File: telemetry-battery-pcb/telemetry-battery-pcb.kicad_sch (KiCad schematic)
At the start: 80 parts, among them J1 Network Connector, J3 360410_MZC, J4 DS18B20, J5 360410_MZC, Q4 2N7002, U4 LTC2944, U5 XR76208, U6 M24C02-WMN, U7 TPS1HTC30-Q1, U8 DS2484R, U9 TPS22969

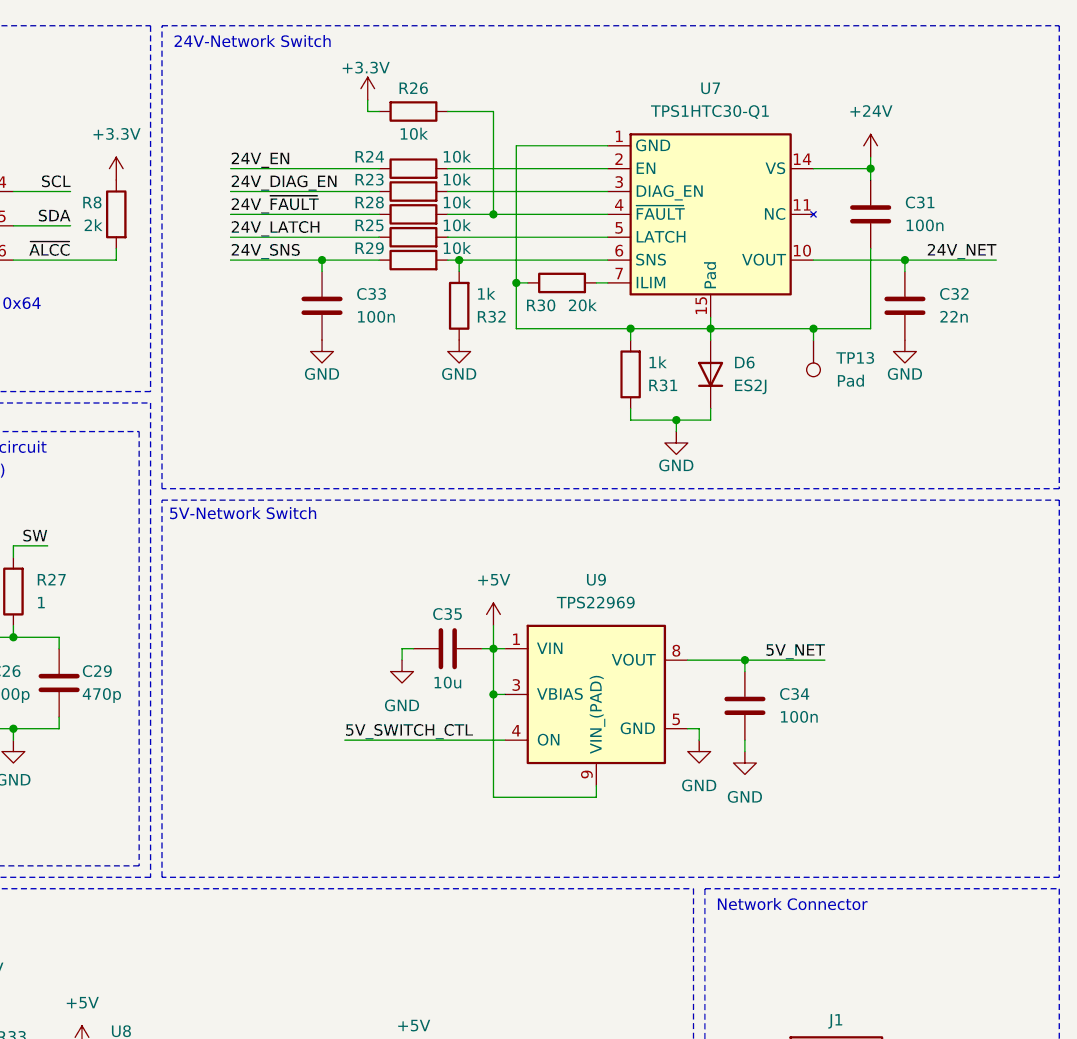
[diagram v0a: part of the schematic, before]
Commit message: telemetry-battery: update of the template according to the Template_Protocolv1.0 available in the exo-template-pcb github the 2026-10-23
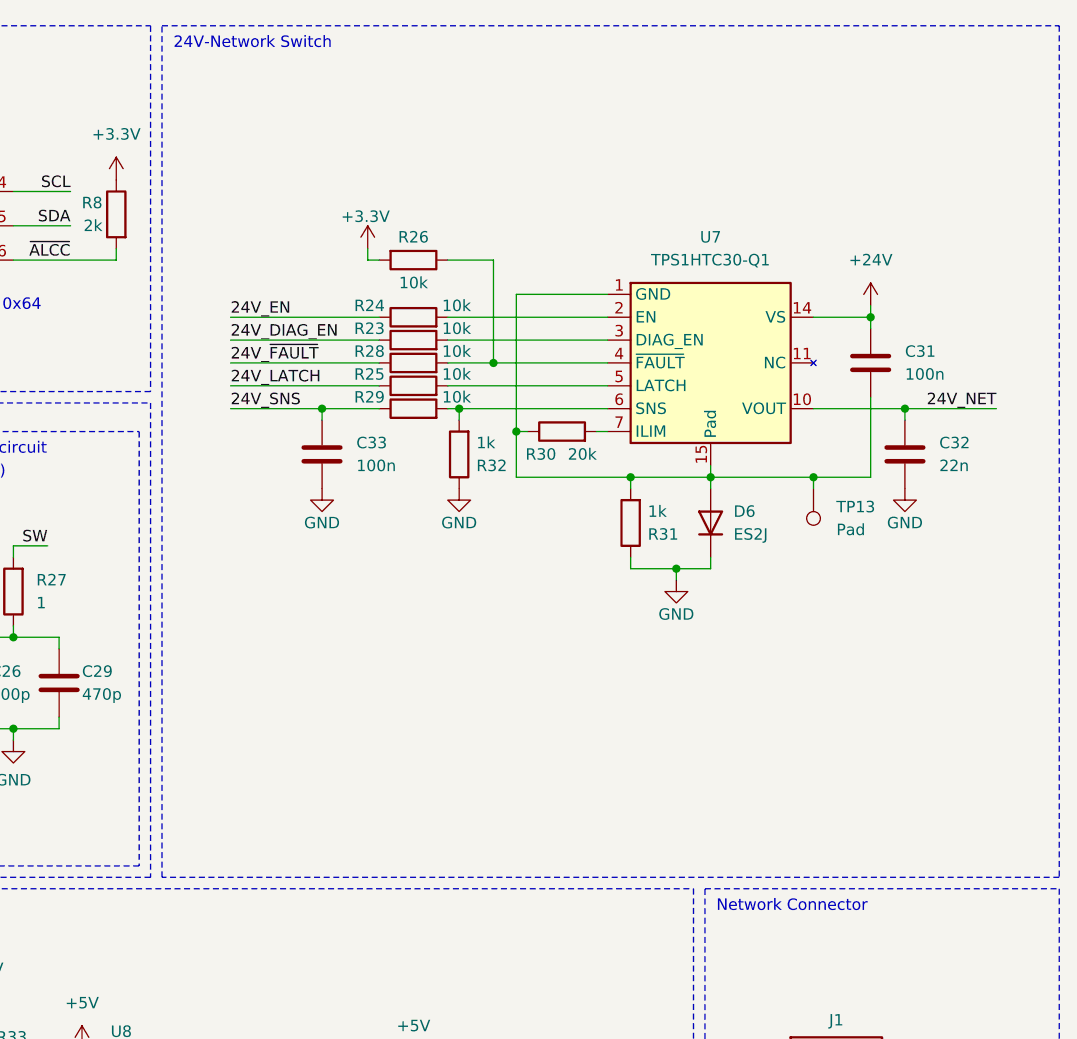
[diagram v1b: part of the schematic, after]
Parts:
- removed C34: 100n, Capacitor_SMD:C_0402_1005Metric, symbol Device:C
- removed C35: 10u, Capacitor_SMD:C_0603_1608Metric, symbol Device:C
- removed U9: TPS22969, Exocet:TPS22969_WSON-8_3x3mm_Thermal_Pad, symbol Exocet:TPS22969
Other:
- note removed: "5V-Network Switch"
- moved on the sheet: C31, C32, C33, D6, R23, R24, R25, R26, R28, R29, R30, R31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

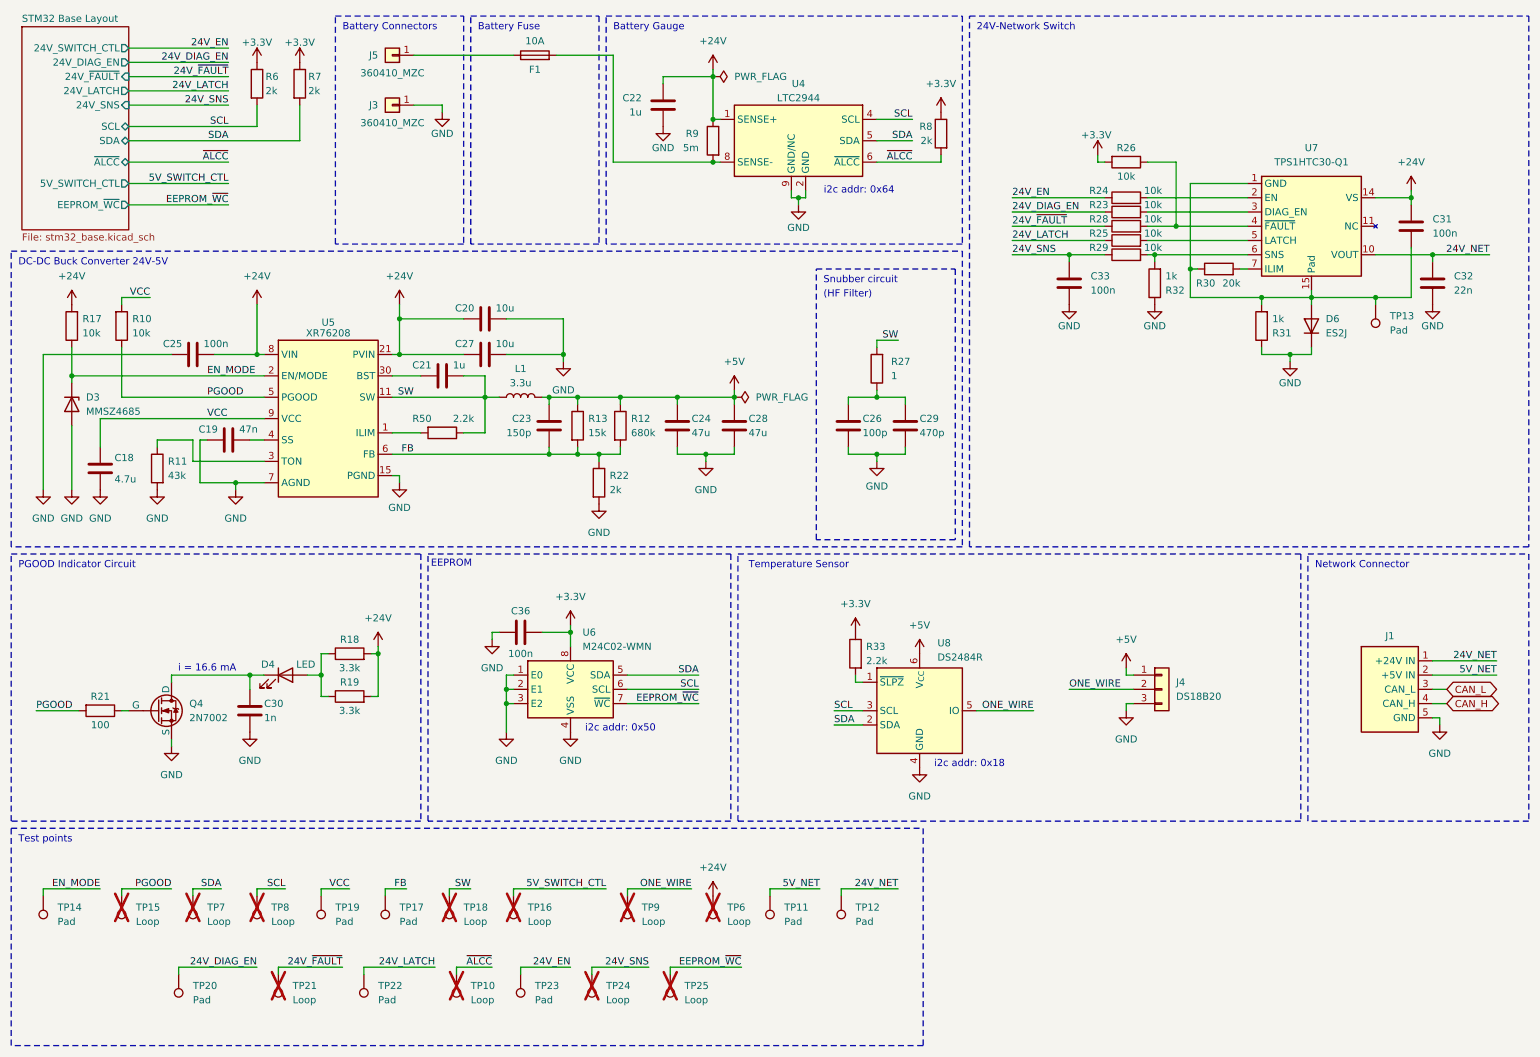
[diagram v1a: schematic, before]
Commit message: telemetry-battery-pcb: update of the schematic with the new stm32 Base Model including removing the 24V converter and switch and associated devices (PGOOD).
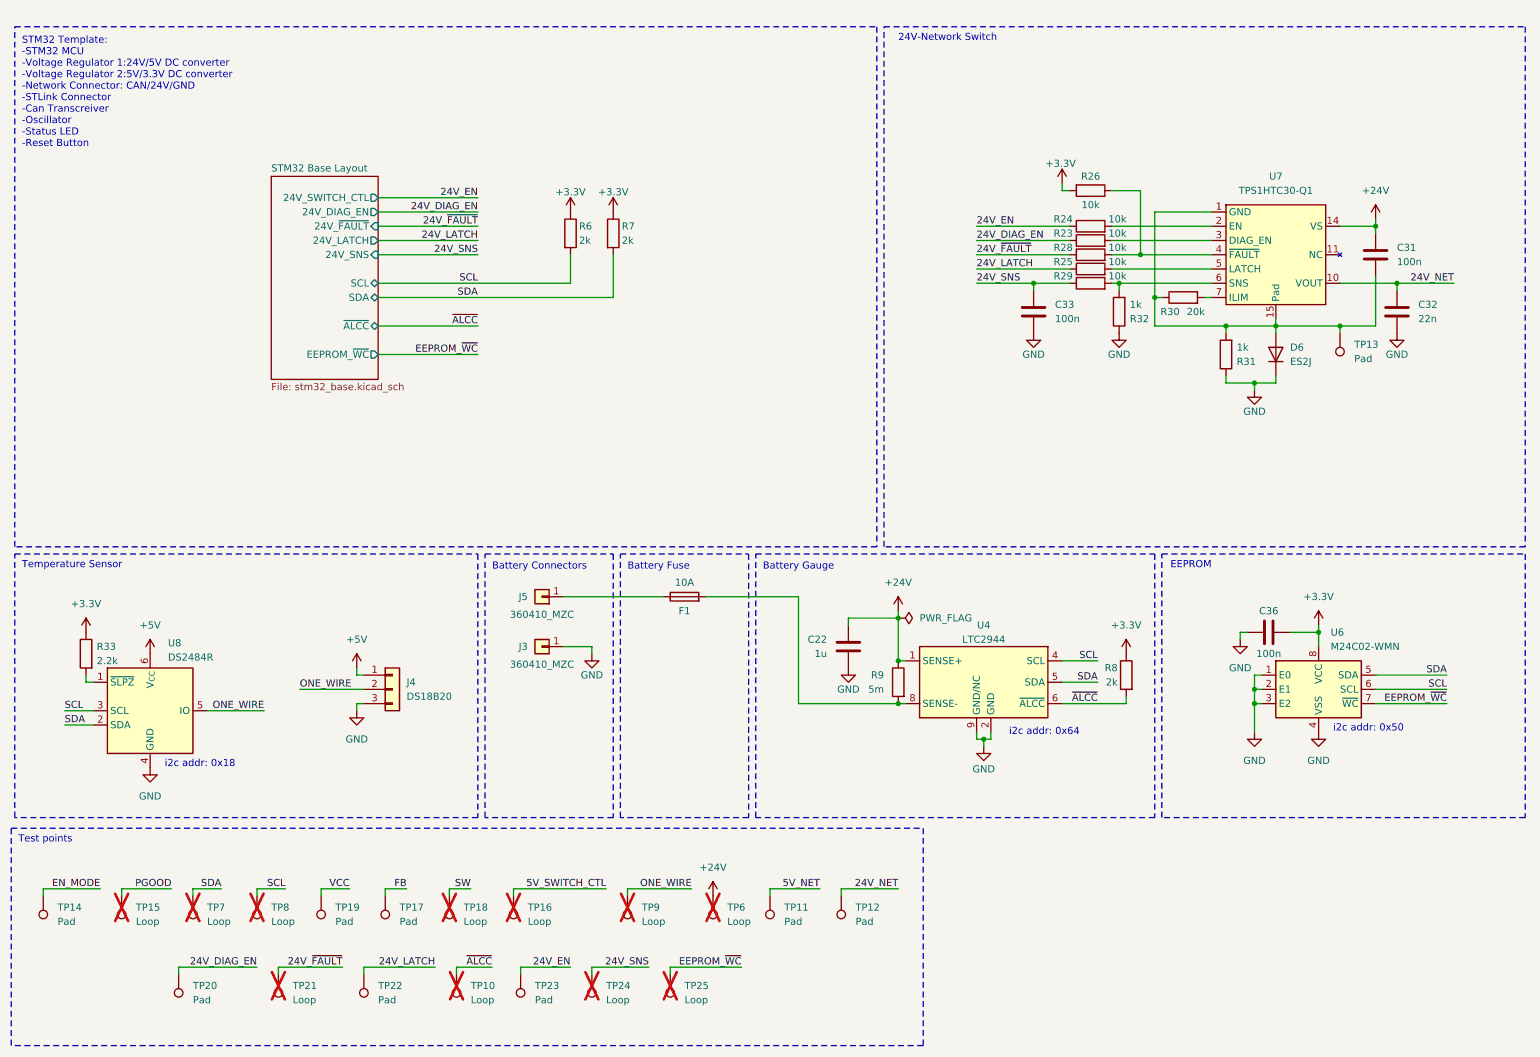
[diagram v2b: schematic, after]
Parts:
- removed C18: 4.7u, Capacitor_SMD:C_0402_1005Metric, symbol Device:C
- removed C19: 47n, Capacitor_SMD:C_0603_1608Metric, symbol Device:C
- removed C20, C27: 10u, Capacitor_SMD:C_1206_3216Metric, symbol Device:C
- removed C21: 1u, Capacitor_SMD:C_0603_1608Metric, symbol Device:C
- removed C23: 150p, Capacitor_SMD:C_0603_1608Metric, symbol Device:C
- removed C24, C28: 47u, Capacitor_SMD:C_1206_3216Metric, symbol Device:C
- removed C25: 100n, Capacitor_SMD:C_0603_1608Metric, symbol Device:C
- removed C26: 100p, Capacitor_SMD:C_0402_1005Metric, symbol Device:C
- removed C29: 470p, Capacitor_SMD:C_0603_1608Metric, symbol Device:C
- removed C30: 1n, Capacitor_SMD:C_0402_1005Metric, symbol Device:C
- removed D3: MMSZ4685, Diode_SMD:D_SOD-123, symbol Device:D_Zener
- removed D4: LED, LED_SMD:LED_0603_1608Metric, symbol Device:LED
- removed J1: Network Connector, Connector_Molex:Molex_SPOX_5268-05A_1x05_P2.50mm_Horizontal, symbol Exocet:Network_Connector
- removed L1: 3.3u, Inductor_SMD:L_Sunlord_MWSA1005S, symbol Device:L
- removed Q4: 2N7002, Package_TO_SOT_SMD:SOT-23, symbol Simulation_SPICE:NMOS
- removed R10, R17: 10k, Resistor_SMD:R_0402_1005Metric, symbol Device:R
- removed R11: 43k, Resistor_SMD:R_0603_1608Metric, symbol Device:R
- removed R12: 680k, Resistor_SMD:R_0805_2012Metric, symbol Device:R
- removed R13: 15k, Resistor_SMD:R_0603_1608Metric, symbol Device:R
- removed R18, R19: 3.3k, Resistor_SMD:R_0805_2012Metric, symbol Device:R
- removed R21: 100, Resistor_SMD:R_1206_3216Metric, symbol Device:R
- removed R22: 2k, Resistor_SMD:R_0402_1005Metric, symbol Device:R
- removed R27: 1, Resistor_SMD:R_0603_1608Metric, symbol Device:R
- removed R50: 2.2k, Resistor_THT:R_Axial_DIN0309_L9.0mm_D3.2mm_P12.70mm_Horizontal, symbol Device:R
- removed U5: XR76208, Exocet:MaxLinear_XR76208ELTR-F_QFN-30(5x5), symbol Exocet:XR76208
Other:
- sheet STM32 Base Layout ports: added none; removed 5V_SWITCH_CTL
- note added: "STM32 Template: -STM32 MCU -Voltage Regulator 1:24V/5V DC converter -Voltage Regulator 2:5V/3.3V DC converter -Network Connector: CAN/24V/GND -STLink Connector -Can Transcreiver -Oscillator -Status LED -Reset Button"
- note removed: "(HF Filter)"
- note removed: "DC-DC Buck Converter 24V-5V"
- note removed: "Network Connector"
- note removed: "PGOOD Indicator Circuit"
- note removed: "Snubber circuit"
- note removed: "i = 16.6 mA"
- company: (none) -> Exocet-Polytechnique
- title: Main Page -> telemetry-battery-pcb
- moved on the sheet: C22, C31, C32, C33, C36, D6, F1, J3, J4, J5, R23, R24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
